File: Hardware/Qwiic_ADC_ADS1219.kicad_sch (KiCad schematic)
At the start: 37 parts, among them J1 Qwiic_RA, J2 Qwiic_RA, J3 Conn_01x06, J4 Conn_01x06, J5 Conn_01x02, J6 I2C_01x04, U1 ADS1219IPW

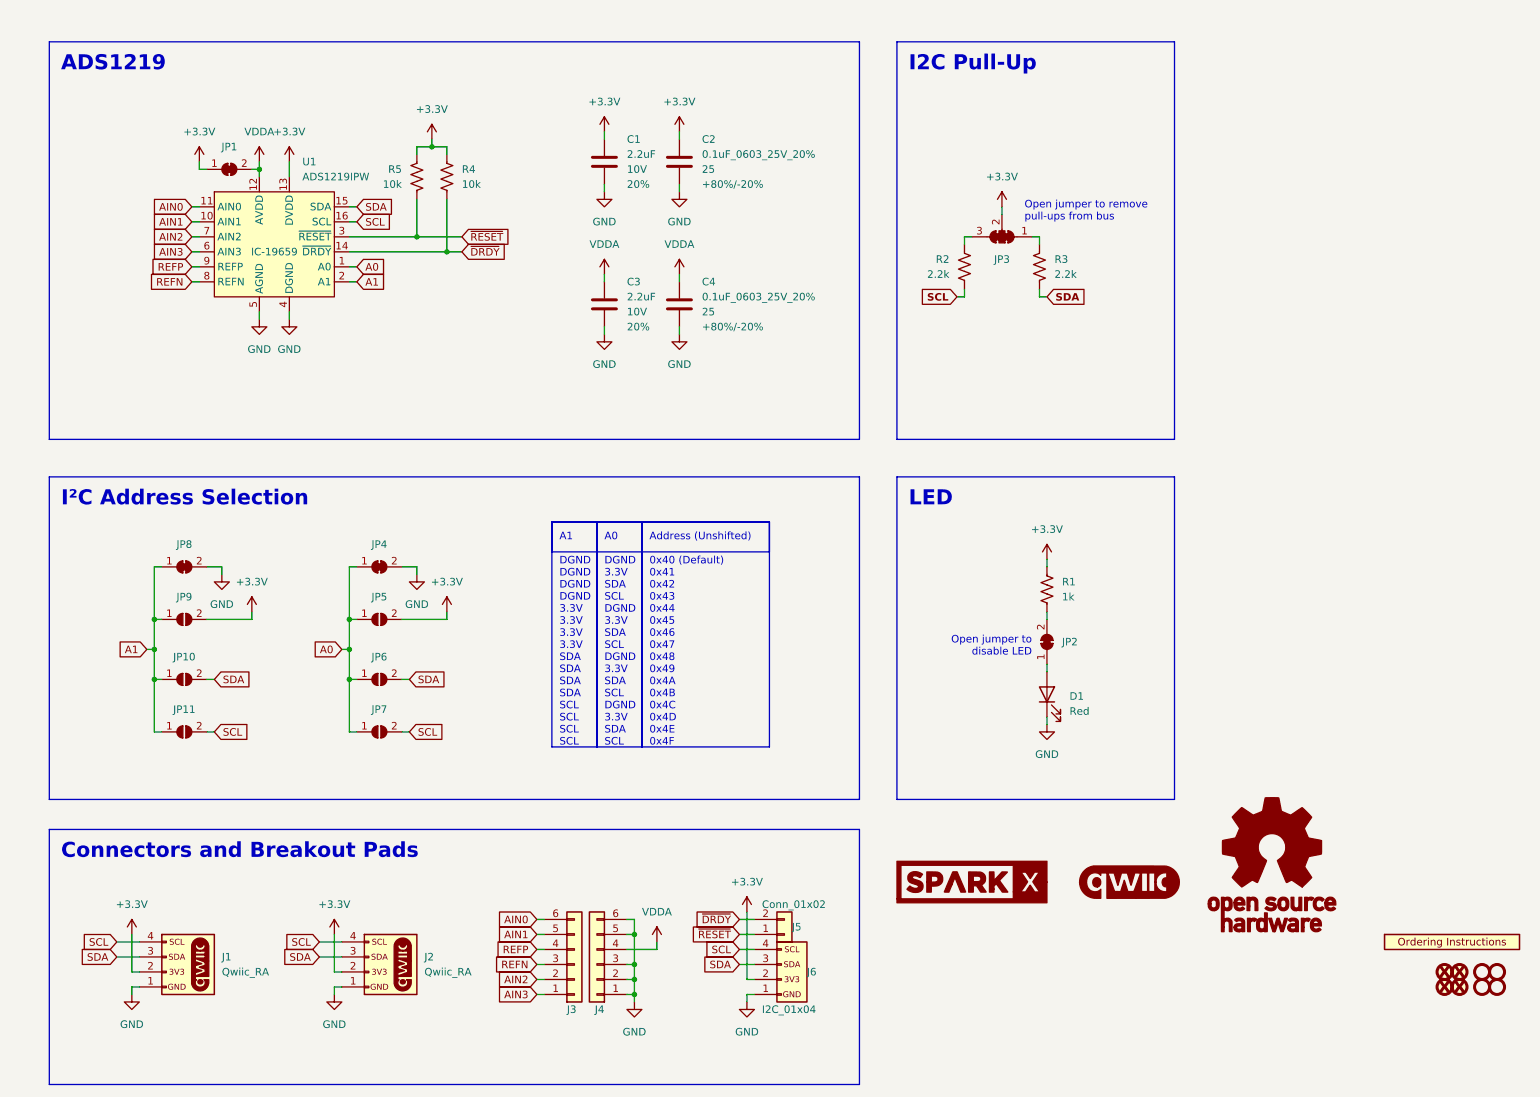
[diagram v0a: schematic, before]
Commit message: Update silk. Change address jumper names.
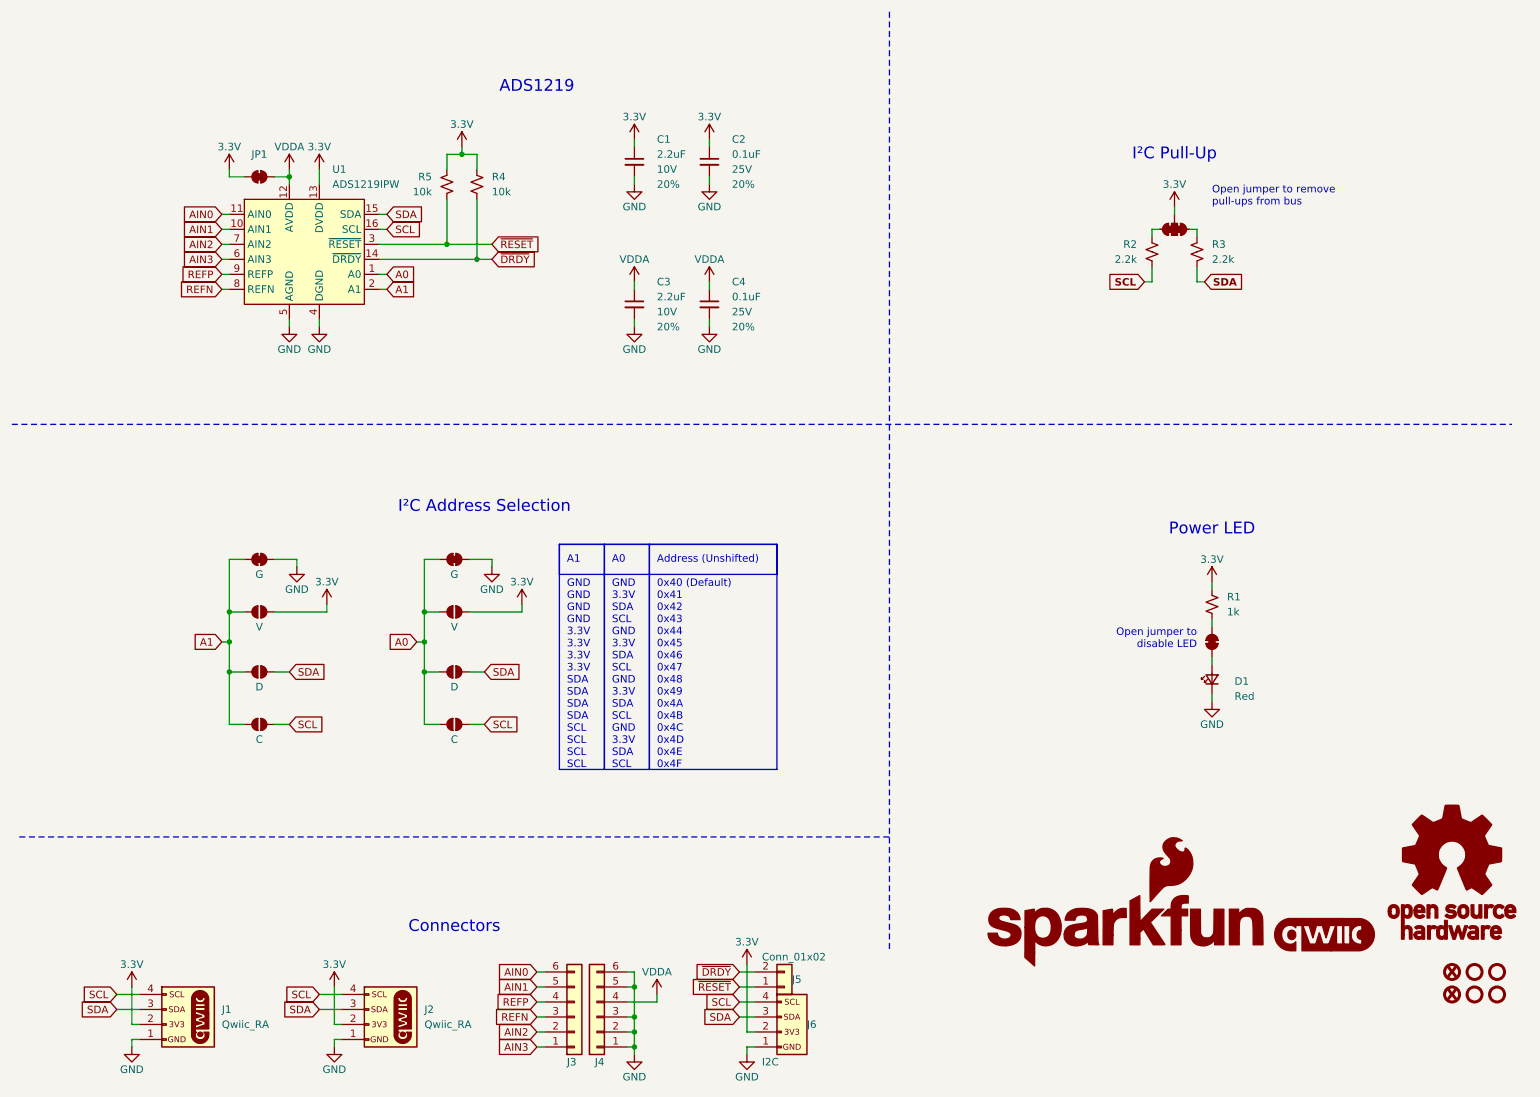
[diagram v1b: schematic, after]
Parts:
- removed FID2, FID4: Fiducial_0.635, SparkFun-Aesthetic:Fiducial_0.635mm, symbol SparkFun-Aesthetic:Fiducial_0.635
- removed U2: ~, SparkFun-Aesthetic:ORDERING_INSTRUCTIONS, symbol SparkFun-Aesthetic:Ordering_Instructions
- added G1: SparkFun_Logo, symbol SparkFun-Aesthetic:SparkFun_Logo
- C2, C4: value 0.1uF_0603_25V_20% -> 0.1uF; Tolerance +80%/-20% -> 20%; Voltage 25 -> 25V
- D1: footprint SparkFun-LED:LED_0603_1608Metric -> SparkFun-LED:LED_0603_1608Metric_Red; PROD_ID DIO-00819 -> DIO-17976
- FID1, FID3: value Fiducial_0.635 -> Fiducial_0.5mm; footprint SparkFun-Aesthetic:Fiducial_0.635mm -> SparkFun-Aesthetic:Fiducial_0.5mm_Mask1mm; symbol SparkFun-Aesthetic:Fiducial_0.635 -> SparkFun-Aesthetic:Fiducial_0.5mm
- J1, J2: footprint SparkFun-Connector:JST04_1MM_RA -> SparkFun-Connector:JST_SMD_1.0mm-4_Black
- J3, J4: footprint SparkFun-Connector:1X06 -> SparkFun-Connector:1x06
- J5: footprint SparkFun-Connector:1X02 -> SparkFun-Connector:1x02
- J6: value I2C_01x04 -> I2C; footprint SparkFun-Connector:1X04 -> SparkFun-Connector:1x04
- JP1, JP2: footprint SparkFun-Jumper:SMT-JUMPER_2_NC_TRACE_SILK -> SparkFun-Jumper:Jumper_2_NC_Trace
- JP10, JP6: value ~ -> D; footprint SparkFun-Jumper:SMT-JUMPER_2_NO_SILK -> SparkFun-Jumper:Jumper_2_NO
- JP11, JP7: value ~ -> C; footprint SparkFun-Jumper:SMT-JUMPER_2_NO_SILK -> SparkFun-Jumper:Jumper_2_NO
- JP3: footprint SparkFun-Jumper:SMT-JUMPER_3_2-NC_TRACE_SILK -> SparkFun-Jumper:Jumper_3_NC-2_Trace
- JP4, JP8: value ~ -> G; footprint SparkFun-Jumper:SMT-JUMPER_2_NC_TRACE_SILK -> SparkFun-Jumper:Jumper_2_NC_Trace
- JP5, JP9: value ~ -> V; footprint SparkFun-Jumper:SMT-JUMPER_2_NO_SILK -> SparkFun-Jumper:Jumper_2_NO
- ST1, ST2, ST3, ST4: value Stand_off -> Standoff; footprint SparkFun-Hardware:STAND-OFF -> SparkFun-Hardware:Standoff; symbol SparkFun-Hardware:Stand_off -> SparkFun-Hardware:Standoff
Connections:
- net SCL: now also R2.1; no longer R2.2
- net ~{DRDY}: now also R4.1; no longer R4.2
- net at J2.NC1 (NC): no longer J2.NC2 (NC)
- net at JP2.2 (B): now also R1.1; no longer R1.2
- net at JP3.3 (C): now also R2.2; no longer R2.1
- net at J1.NC1 (NC): no longer J1.NC2 (NC)
- net +3.3V renamed 3.3V
- net 3.3V: now also R1.2, R4.2; no longer R1.1, R4.1
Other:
- note added: "A0 GND 3.3V SDA SCL GND 3.3V SDA SCL GND 3.3V SDA SCL GND 3.3V SDA SCL"
- note added: "A1 GND GND GND GND 3.3V 3.3V 3.3V 3.3V SDA SDA SDA SDA SCL SCL SCL SCL"
- note added: "ADS1219"
- note added: "Connectors"
- note added: "I²C Address Selection"
- note added: "I²C Pull-Up"
- note added: "Power LED"
- note removed: "A0 DGND 3.3V SDA SCL DGND 3.3V SDA SCL DGND 3.3V SDA SCL DGND 3.3V SDA SCL"
- note removed: "A1 DGND DGND DGND DGND 3.3V 3.3V 3.3V 3.3V SDA SDA SDA SDA SCL SCL SCL SCL"
- company: (none) -> SparkFun Electronics
- title: SparkX ADC ADS1219 (Qwiic) -> SparkFun ADC ADS1219 (Qwiic)
- moved on the sheet: C1, C2, C3, C4, D1, J1, J2, J3, J4, J5, J6, U1
